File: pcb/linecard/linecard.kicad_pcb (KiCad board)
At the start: 6 copper layers, 185 x 93.5 mm, 624 parts, among them J1 CONN_ATX12V, J10 ARF6-08-S-D-A-K-TR, J11 SMPM, J12 SMPM, J13 XILINX_JTAG, J14 ARF6-08-S-D-A-K-TR, J2 LPJT476156AENL, J3 CORTEX_DEBUG_ETM, J4 0532611071, J5 LPJT476156AENL, J6 XILINX_JTAG, J7 SMPM, J8 SMPM, J9 LPJT476156AENL, M1 LONGTHING, M10 SCREWHOLE, M11 SCREWHOLE, M12 960-27-12-D-AB-0, M13 960-27-12-D-AB-0, M2 OSHW, M3 WEEE, M4 SCREWHOLE, M5 SCREWHOLE, M6 SCREWHOLE, M7 SCREWHOLE, M8 SCREWHOLE, M9 SCREWHOLE, SW1 SWITCH, SW2 SWITCH, U1 MYMGK00504ERSR, U10 VSC8512, U11 ESD224DQAR, U12 ESD224DQAR, U13 ESD224DQAR, U14 ESD224DQAR, U15 ESD224DQAR, U16 ESD224DQAR, U17 ESD224DQAR, U18 ESD224DQAR, U19 ESD224DQAR, U2 MYMGK00504ERSR, U20 ESD224DQAR, U21 ESD224DQAR, U22 ESD224DQAR, U23 ESD224DQAR, U24 ESD224DQAR, U25 ESD224DQAR, U26 ESD224DQAR, U27 ESD224DQAR, U28 ESD224DQAR, U29 ESD224DQAR, U3 MYMGK00504ERSR, U30 ESD224DQAR, U31 ESD224DQAR, U32 ESD224DQAR, U33 ESD224DQAR, U34 ESD224DQAR, U35 VSC8512, U36 ESD224DQAR, U37 ESD224DQAR, U38 ESD224DQAR, U39 ESD224DQAR, U4 MYMGK00504ERSR, U40 ESD224DQAR, U41 ESD224DQAR, U42 ESD224DQAR, U43 ESD224DQAR, U44 ESD224DQAR, U45 ESD224DQAR, U46 ESD224DQAR, U47 ESD224DQAR, U48 ESD224DQAR, U49 ESD224DQAR, U5 STM32L431-QFN48, U50 ESD224DQAR, U51 ESD224DQAR, U52 ESD224DQAR, U53 ESD224DQAR, U54 ESD224DQAR, U55 ESD224DQAR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

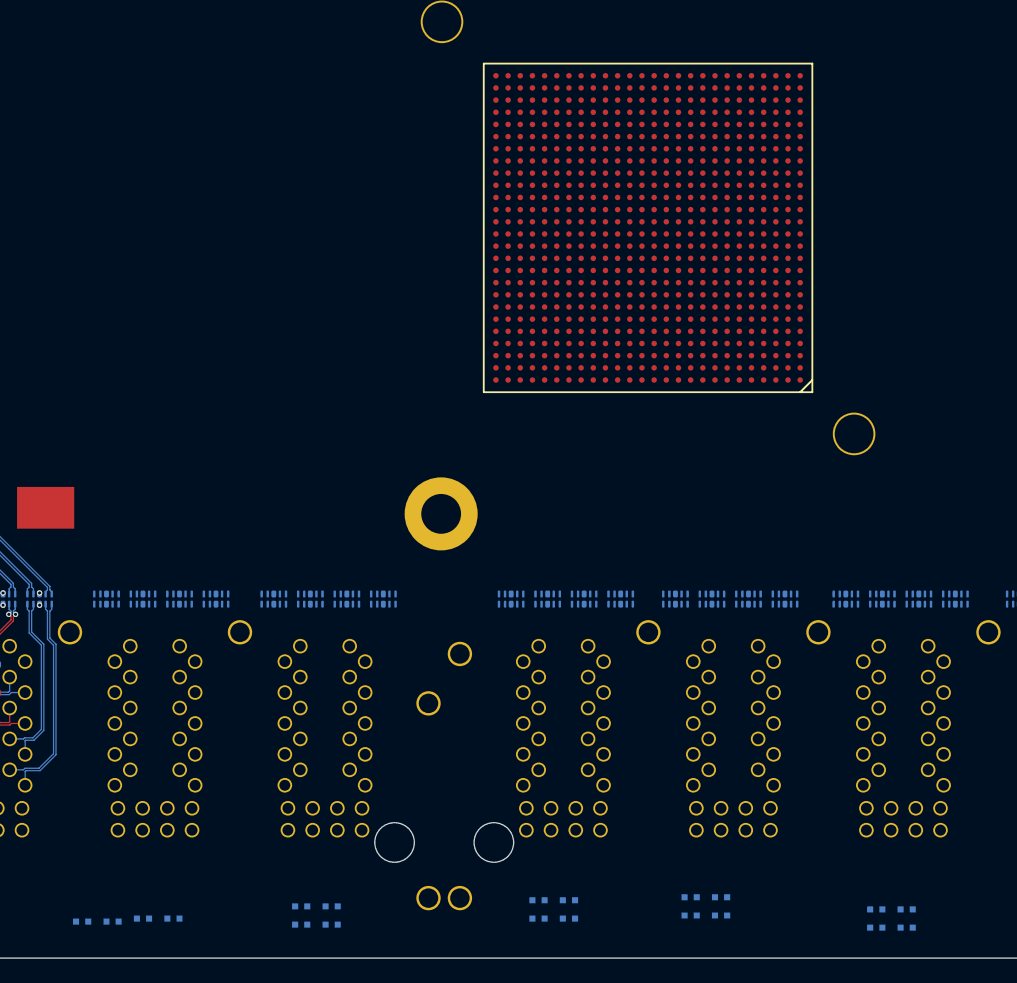
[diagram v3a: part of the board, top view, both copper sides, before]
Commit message: Began routing right side VSC8512
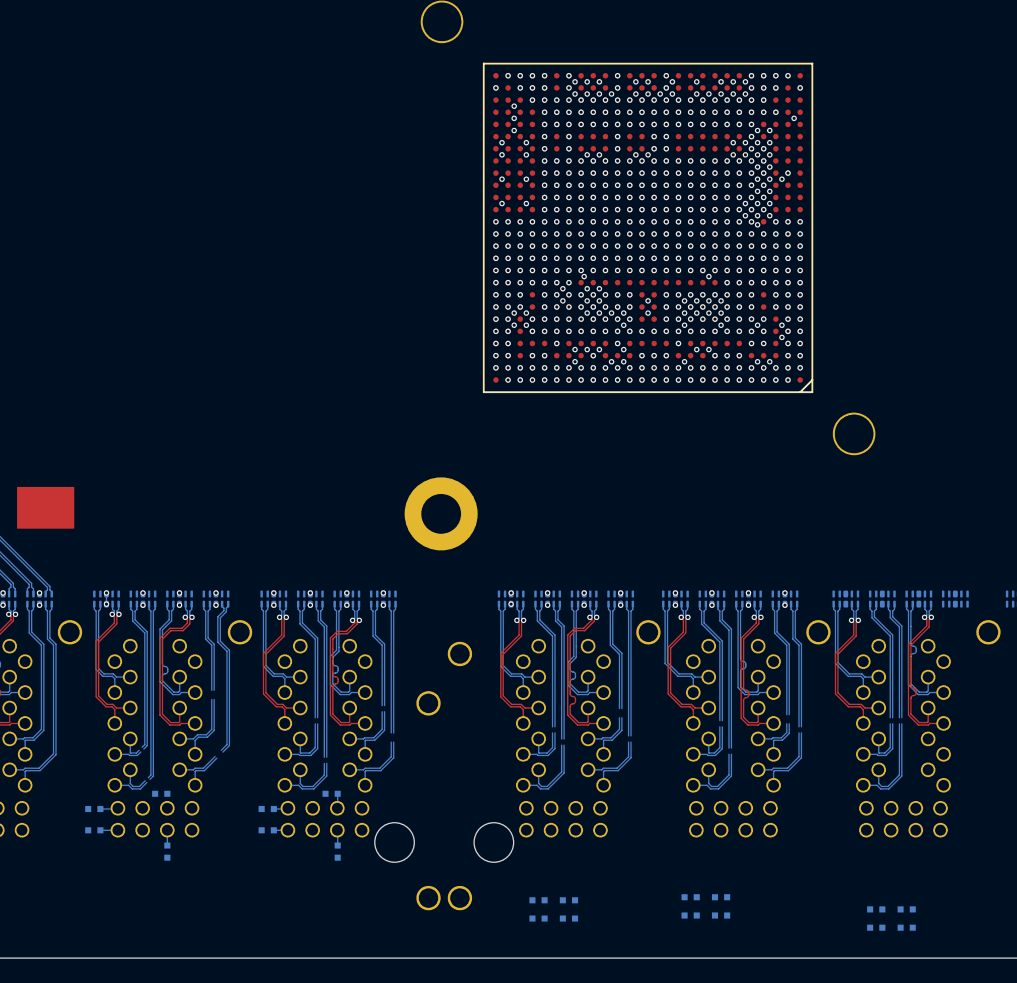
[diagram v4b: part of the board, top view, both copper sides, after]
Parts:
- moved R80 12.3 mm to (129.0, 135.0)
- moved R69 11.1 mm to (123.5, 136.2)
- moved R71 10.9 mm to (137.8, 136.2)
- moved R82 9.58 mm to (143.0, 135.0)
- moved R70 8.16 mm to (137.8, 138.0)
- moved R68 7.65 mm to (123.5, 138.0)
- moved R83 6.71 mm to (143.5, 139.7), turned to -90 degrees
- moved R81 5.85 mm to (129.5, 139.8), turned to -90 degrees
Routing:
- net /GND: track 1191.0 -> 1491.8 mm, vias 382 -> 658
- net /1V0: track 118.7 -> 202.7 mm, vias 88 -> 170
- net /PHY 1 MDI/PHY2_M0_P: track 0.00 -> 17.9 mm
- net /PHY 1 MDI/PHY8_M0_P: track 0.00 -> 17.7 mm
- net /PHY 1 MDI/PHY6_M0_P: track 0.00 -> 17.7 mm
- net /PHY 1 MDI/PHY4_M0_P: track 0.00 -> 17.7 mm
- net /PHY 1 MDI/PHY2_M0_N: track 0.00 -> 17.4 mm
- net /PHY 1 MDI/PHY0_M0_P: track 0.00 -> 17.4 mm
- net /PHY 1 MDI/PHY0_M0_N: track 0.00 -> 17.2 mm
- net /PHY 1 MDI/PHY8_M0_N: track 0.00 -> 17.2 mm
- net /PHY 1 MDI/PHY6_M0_N: track 0.00 -> 17.2 mm
- net /PHY 1 MDI/PHY4_M0_N: track 0.00 -> 17.2 mm
- net /PHY 1 MDI/PHY1_M0_N: track 0.00 -> 16.3 mm
- net /PHY 1 MDI/PHY7_M0_P: track 0.00 -> 16.3 mm
- net /PHY 1 MDI/PHY1_M0_P: track 0.00 -> 16.2 mm
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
